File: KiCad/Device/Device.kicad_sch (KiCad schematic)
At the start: 23 parts, among them IC1 ATTINY167-XUR, J1 Mikrofon, J2 Lysføler, J3 Optisk sensor, J4 Fugtføler, J5 VCC, J6 ESP8266(wifi), SW1 Reset, SW2 Button01, SW3 SW_DIP_x01, Y1 Crystal

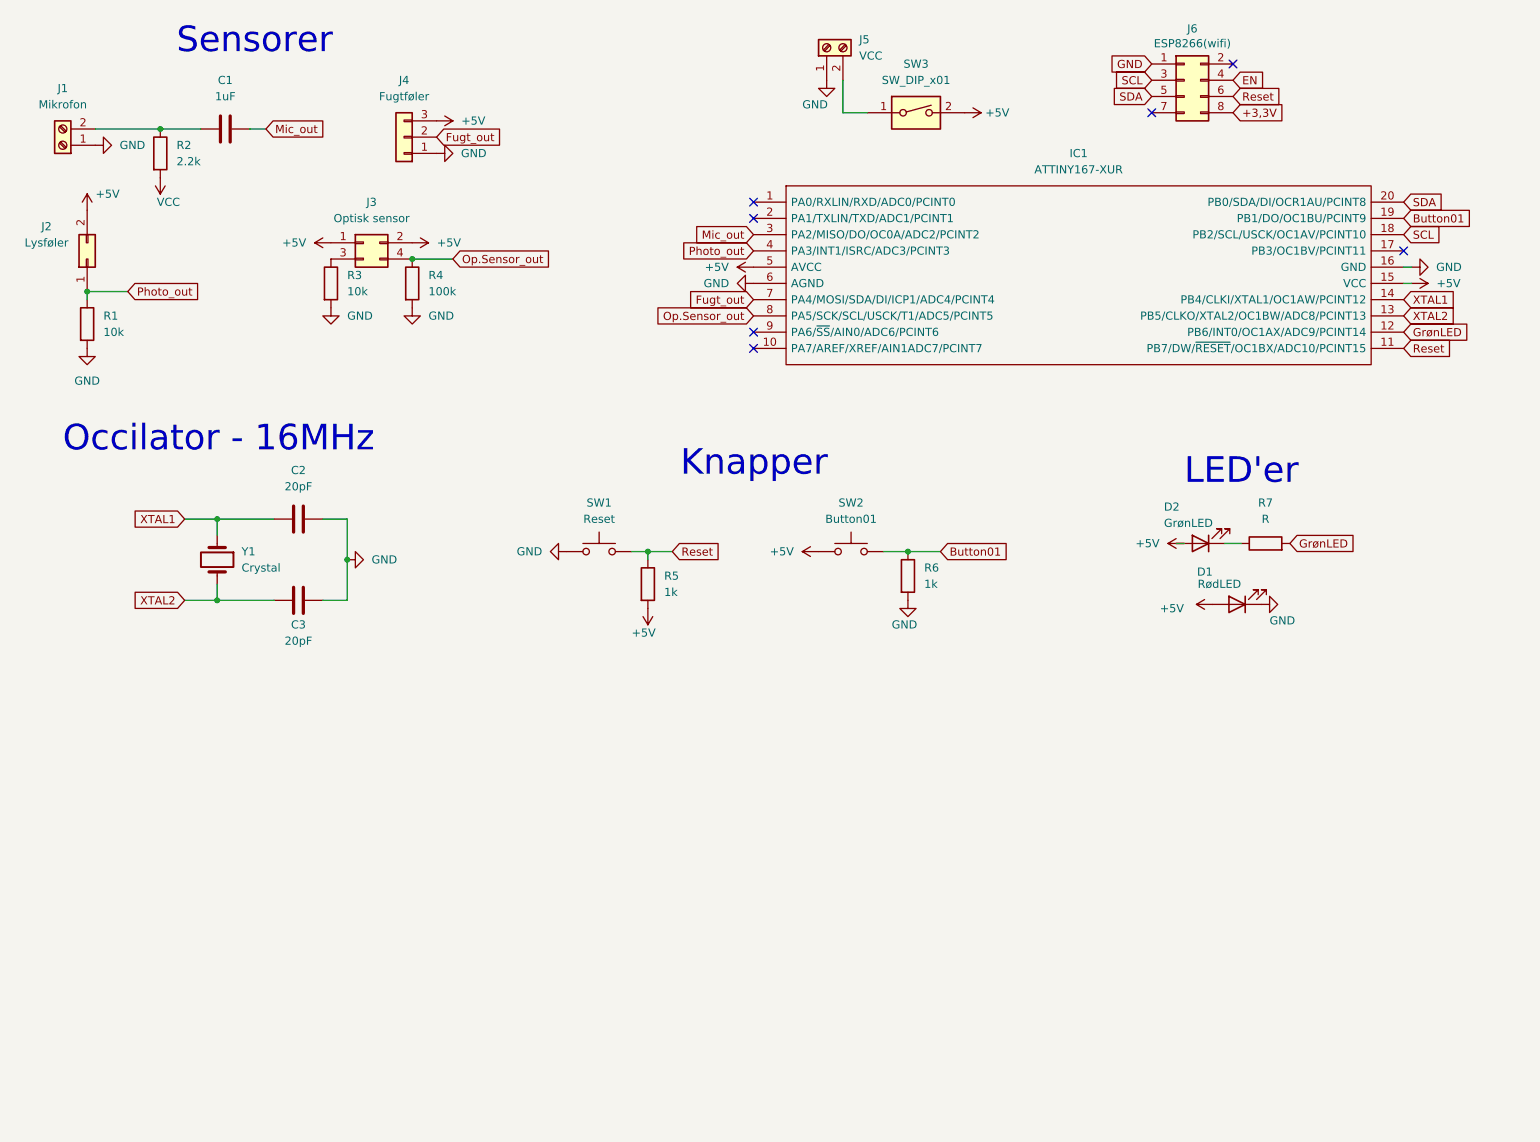
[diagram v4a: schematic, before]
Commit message: Opdatering af device kicad
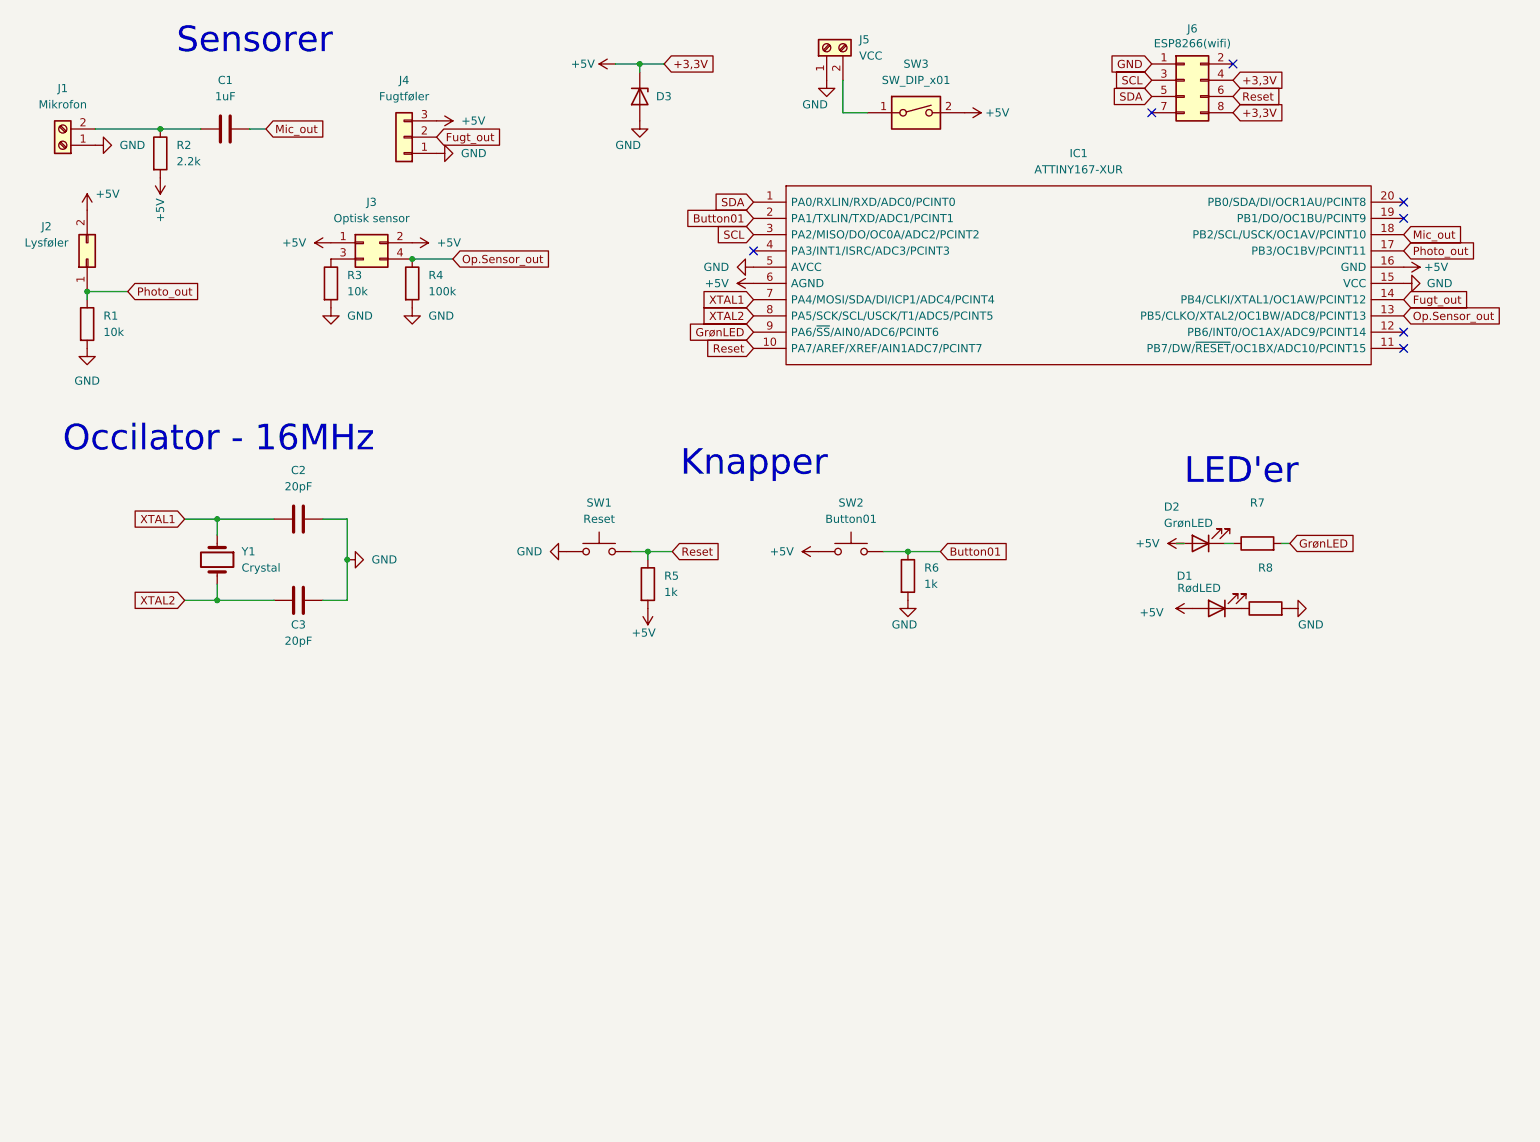
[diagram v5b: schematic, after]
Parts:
- added D3: (no value), symbol Device:D_Zener
- added R8: (no value), Resistor_THT:R_Axial_DIN0309_L9.0mm_D3.2mm_P12.70mm_Horizontal, symbol Device:R
- C1, C2, C3: footprint (none) -> Capacitor_THT:C_Disc_D5.0mm_W2.5mm_P5.00mm
- D1, D2: footprint (none) -> LED_THT:LED_D3.0mm_FlatTop
- IC1: footprint victorkicad:SOIC127P1034X264-20N -> (none)
- J1, J5: footprint (none) -> Connector_Phoenix_MC_HighVoltage:PhoenixContact_MCV_1,5_2-G-5.08_1x02_P5.08mm_Vertical
- J2: footprint (none) -> Connector_PinSocket_2.54mm:PinSocket_2x01_P2.54mm_Vertical
- J3: footprint (none) -> Connector_PinSocket_2.54mm:PinSocket_2x02_P2.54mm_Vertical
- J4: footprint (none) -> Connector_PinSocket_2.54mm:PinSocket_1x03_P2.54mm_Vertical
- J6: footprint (none) -> Connector_PinSocket_2.54mm:PinSocket_2x04_P2.54mm_Vertical
- R1, R2, R3, R4, R5, R6: footprint (none) -> Resistor_THT:R_Axial_DIN0309_L9.0mm_D3.2mm_P12.70mm_Horizontal
- R7: value R -> (none); footprint (none) -> Resistor_THT:R_Axial_DIN0309_L9.0mm_D3.2mm_P12.70mm_Horizontal
- SW1, SW2: footprint Button_Switch_SMD:SW_MEC_5GSH9 -> Button_Switch_THT:SW_PUSH_6mm_H4.3mm
- SW3: footprint (none) -> Button_Switch_THT:SW_DIP_SPSTx02_Slide_9.78x7.26mm_W7.62mm_P2.54mm
- Y1: footprint (none) -> Crystal:Crystal_HC18-U_Vertical
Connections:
- net +3,3V is gone; now on net +5V: J6.8 (Pin_8)
- net EN is gone; now on net +5V: J6.4 (Pin_4)
- net VCC is gone; now on net +5V: R2.2
- net +5V: now also IC1.16 (GND), IC1.6 (AGND), D3.1 (K); no longer IC1.15 (VCC), IC1.5 (AVCC)
- net Button01: now also IC1.2 (PA1/TXLIN/TXD/ADC1/PCINT1); no longer IC1.19 (PB1/DO/OC1BU/PCINT9)
- net Fugt_out: now also IC1.14 (PB4/CLKI/XTAL1/OC1AW/PCINT12); no longer IC1.7 (PA4/MOSI/SDA/DI/ICP1/ADC4/PCINT4)
- net GND: now also IC1.15 (VCC), IC1.5 (AVCC), D3.2 (A), R8.2; no longer D1.1 (K), IC1.16 (GND), IC1.6 (AGND)
- net GrønLED: now also IC1.9 (PA6/~{SS}/AIN0/ADC6/PCINT6); no longer IC1.12 (PB6/INT0/OC1AX/ADC9/PCINT14)
- net Mic_out: now also IC1.18 (PB2/SCL/USCK/OC1AV/PCINT10); no longer IC1.3 (PA2/MISO/DO/OC0A/ADC2/PCINT2)
- net Op.Sensor_out: now also IC1.13 (PB5/CLKO/XTAL2/OC1BW/ADC8/PCINT13); no longer IC1.8 (PA5/SCK/SCL/USCK/T1/ADC5/PCINT5)
- net Photo_out: now also IC1.17 (PB3/OC1BV/PCINT11); no longer IC1.4 (PA3/INT1/ISRC/ADC3/PCINT3)
- net Reset: now also IC1.10 (PA7/AREF/XREF/AIN1ADC7/PCINT7); no longer IC1.11 (PB7/DW/~{RESET}/OC1BX/ADC10/PCINT15)
- net SCL: now also IC1.3 (PA2/MISO/DO/OC0A/ADC2/PCINT2); no longer IC1.18 (PB2/SCL/USCK/OC1AV/PCINT10)
- net SDA: now also IC1.1 (PA0/RXLIN/RXD/ADC0/PCINT0); no longer IC1.20 (PB0/SDA/DI/OCR1AU/PCINT8)
- net XTAL1: now also IC1.7 (PA4/MOSI/SDA/DI/ICP1/ADC4/PCINT4); no longer IC1.14 (PB4/CLKI/XTAL1/OC1AW/PCINT12)
- net XTAL2: now also IC1.8 (PA5/SCK/SCL/USCK/T1/ADC5/PCINT5); no longer IC1.13 (PB5/CLKO/XTAL2/OC1BW/ADC8/PCINT13)
- new net: D1.1 (K), R8.1
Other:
- moved on the sheet: D1, R7

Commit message: Minor fixes
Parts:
- added C4: C, symbol Device:C
- added R9: 10-20ohm, Resistor_THT:R_Axial_DIN0309_L9.0mm_D3.2mm_P12.70mm_Horizontal, symbol Device:R
- D3: value (none) -> BZX79C3V3; footprint (none) -> Diode_SMD:D_MELF_Handsoldering
- IC1: footprint (none) -> Package_DIP:DIP-20_W7.62mm_Socket
- R7, R8: value (none) -> 200
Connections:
- net +5V: now also IC1.15 (AGND), IC1.5 (GND), R9.1; no longer D3.1 (K), IC1.16 (GND), IC1.6 (AGND), J6.4 (Pin_4), J6.8 (Pin_8)
- net Button01: now also IC1.19 (PA1/TXLIN/TXD/ADC1/PCINT1); no longer IC1.2 (PA1/TXLIN/TXD/ADC1/PCINT1)
- net Fugt_out: now also IC1.7 (PB4/CLKI/XTAL1/OC1AW/PCINT12); no longer IC1.14 (PB4/CLKI/XTAL1/OC1AW/PCINT12)
- net GND: now also IC1.16 (AVCC), IC1.6 (VCC), C4.2; no longer IC1.15 (VCC), IC1.5 (AVCC)
- net GrønLED: now also IC1.12 (PA6/~{SS}/AIN0/ADC6/PCINT6); no longer IC1.9 (PA6/~{SS}/AIN0/ADC6/PCINT6)
- net Mic_out: now also IC1.3 (PB2/SCL/USCK/OC1AV/PCINT10); no longer IC1.18 (PB2/SCL/USCK/OC1AV/PCINT10)
- net Op.Sensor_out: now also IC1.8 (PB5/CLKO/XTAL2/OC1BW/ADC8/PCINT13); no longer IC1.13 (PB5/CLKO/XTAL2/OC1BW/ADC8/PCINT13)
- net Photo_out: now also IC1.4 (PB3/OC1BV/PCINT11); no longer IC1.17 (PB3/OC1BV/PCINT11)
- net Reset: now also IC1.11 (PA7/AREF/XREF/AIN1ADC7/PCINT7); no longer IC1.10 (PA7/AREF/XREF/AIN1ADC7/PCINT7)
- net SCL: now also IC1.18 (PA2/MISO/DO/OC0A/ADC2/PCINT2); no longer IC1.3 (PA2/MISO/DO/OC0A/ADC2/PCINT2)
- net SDA: now also IC1.20 (PA0/RXLIN/RXD/ADC0/PCINT0); no longer IC1.1 (PA0/RXLIN/RXD/ADC0/PCINT0)
- net XTAL1: now also IC1.14 (PA4/MOSI/SDA/DI/ICP1/ADC4/PCINT4); no longer IC1.7 (PA4/MOSI/SDA/DI/ICP1/ADC4/PCINT4)
- net XTAL2: now also IC1.13 (PA5/SCK/SCL/USCK/T1/ADC5/PCINT5); no longer IC1.8 (PA5/SCK/SCL/USCK/T1/ADC5/PCINT5)
- new net +3,3V: C4.1, D3.1 (K), J6.4 (Pin_4), J6.8 (Pin_8), R9.2
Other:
- note added: "Strømforsyning"
- moved on the sheet: C2, C3, D1, D2, D3, J5, J6, R5, R6, R7, R8, SW1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

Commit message: fix ic
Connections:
- net +5V: now also IC1.16 (AVCC), IC1.6 (VCC); no longer IC1.15 (AGND), IC1.5 (GND)
- net Button01: now also IC1.2 (PB1/DO/OC1BU/PCINT9); no longer IC1.19 (PA1/TXLIN/TXD/ADC1/PCINT1)
- net Fugt_out: now also IC1.14 (PA4/MOSI/SDA/DI/ICP1/ADC4/PCINT4); no longer IC1.7 (PB4/CLKI/XTAL1/OC1AW/PCINT12)
- net GND: now also IC1.15 (AGND), IC1.5 (GND); no longer IC1.16 (AVCC), IC1.6 (VCC)
- net GrønLED: now also IC1.9 (PB6/INT0/OC1AX/ADC9/PCINT14); no longer IC1.12 (PA6/~{SS}/AIN0/ADC6/PCINT6)
- net Mic_out: now also IC1.18 (PA2/MISO/DO/OC0A/ADC2/PCINT2); no longer IC1.3 (PB2/SCL/USCK/OC1AV/PCINT10)
- net Op.Sensor_out: now also IC1.13 (PA5/SCK/SCL/USCK/T1/ADC5/PCINT5); no longer IC1.8 (PB5/CLKO/XTAL2/OC1BW/ADC8/PCINT13)
- net Photo_out: now also IC1.17 (PA3/INT1/ISRC/ADC3/PCINT3); no longer IC1.4 (PB3/OC1BV/PCINT11)
- net Reset: now also IC1.10 (PB7/DW/~{RESET}/OC1BX/ADC10/PCINT15); no longer IC1.11 (PA7/AREF/XREF/AIN1ADC7/PCINT7)
- net SCL: now also IC1.3 (PB2/SCL/USCK/OC1AV/PCINT10); no longer IC1.18 (PA2/MISO/DO/OC0A/ADC2/PCINT2)
- net SDA: now also IC1.1 (PB0/SDA/DI/OCR1AU/PCINT8); no longer IC1.20 (PA0/RXLIN/RXD/ADC0/PCINT0)
- net XTAL1: now also IC1.7 (PB4/CLKI/XTAL1/OC1AW/PCINT12); no longer IC1.14 (PA4/MOSI/SDA/DI/ICP1/ADC4/PCINT4)
- net XTAL2: now also IC1.8 (PB5/CLKO/XTAL2/OC1BW/ADC8/PCINT13); no longer IC1.13 (PA5/SCK/SCL/USCK/T1/ADC5/PCINT5)
